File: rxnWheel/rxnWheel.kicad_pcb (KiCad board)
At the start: 2 copper layers, 1 part, among them IC1 TB9061AFNG,EL

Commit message: .
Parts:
- added D2: BZV55B12, Diode_SMD:D_MiniMELF, F.Cu at (208.8, 71.1)
- added D3: BZV55B12, Diode_SMD:D_MiniMELF, F.Cu at (200.3, 84.0)
- added D4: BZV55B12, Diode_SMD:D_MiniMELF, F.Cu at (247.5, 71.1)
- added D5: BZV55B12, Diode_SMD:D_MiniMELF, F.Cu at (239.0, 84.0)
- added D6: BZV55B12, Diode_SMD:D_MiniMELF, F.Cu at (228.1, 71.1)
- added D7: BZV55B12, Diode_SMD:D_MiniMELF, F.Cu at (219.7, 84.0)
- added Q1: IRF7458, Package_SO:SOIC-8_3.9x4.9mm_P1.27mm, F.Cu at (169.4, 72.7)
- added Q2: IRF7404, Package_SO:SOIC-8_3.9x4.9mm_P1.27mm, F.Cu at (201.4, 79.2)
- added Q3: Si4162DY, Package_SO:SOIC-8_3.9x4.9mm_P1.27mm, F.Cu at (201.4, 72.7)
- added Q4: IRF7404, Package_SO:SOIC-8_3.9x4.9mm_P1.27mm, F.Cu at (240.1, 79.2)
- added Q5: Si4162DY, Package_SO:SOIC-8_3.9x4.9mm_P1.27mm, F.Cu at (240.1, 72.7)
- added Q6: IRF7404, Package_SO:SOIC-8_3.9x4.9mm_P1.27mm, F.Cu at (220.7, 79.2)
- added Q7: Si4162DY, Package_SO:SOIC-8_3.9x4.9mm_P1.27mm, F.Cu at (220.7, 72.7)
- added R1: 100, Resistor_SMD:R_0805_2012Metric, F.Cu at (207.0, 91.3)
- added R10: 4K, Resistor_SMD:R_0805_2012Metric, F.Cu at (185.0, 73.9)
- added R11: 10K, Resistor_SMD:R_0805_2012Metric, F.Cu at (202.6, 94.3)
- added R12: 10K, Resistor_SMD:R_0805_2012Metric, F.Cu at (198.2, 91.3)
- added R13: 10K, Resistor_SMD:R_0805_2012Metric, F.Cu at (189.4, 71.0)
- added R14: 10K, Resistor_SMD:R_0805_2012Metric, F.Cu at (184.2, 71.0)
- added R15: 1K, Resistor_SMD:R_0805_2012Metric, F.Cu at (202.6, 97.2)
- added R16: 100, Resistor_SMD:R_0805_2012Metric, F.Cu at (202.6, 104.6)
- added R17: 100, Resistor_SMD:R_0805_2012Metric, F.Cu at (198.2, 107.6)
- added R18: 10K, Resistor_SMD:R_0805_2012Metric, F.Cu at (202.6, 107.6)
- added R19: 10K, Resistor_SMD:R_0805_2012Metric, F.Cu at (198.2, 104.6)
- added R2: 10K, Resistor_SMD:R_0805_2012Metric, F.Cu at (198.2, 94.3)
- added R20: 10K, Resistor_SMD:R_0805_2012Metric, F.Cu at (207.0, 104.6)
- added R21: 100, Resistor_SMD:R_0805_2012Metric, F.Cu at (221.1, 104.6)
- added R22: 100, Resistor_SMD:R_0805_2012Metric, F.Cu at (216.7, 107.6)
- added R23: 10K, Resistor_SMD:R_0805_2012Metric, F.Cu at (221.1, 107.6)
- added R24: 10K, Resistor_SMD:R_0805_2012Metric, F.Cu at (216.7, 104.6)
- added R25: 10K, Resistor_SMD:R_0805_2012Metric, F.Cu at (225.5, 104.6)
- added R26: 100, Resistor_SMD:R_0805_2012Metric, F.Cu at (223.9, 91.3)
- added R27: 100, Resistor_SMD:R_0805_2012Metric, F.Cu at (219.5, 94.3)
- added R28: 10K, Resistor_SMD:R_0805_2012Metric, F.Cu at (223.9, 94.3)
- added R29: 10K, Resistor_SMD:R_0805_2012Metric, F.Cu at (219.5, 91.3)
- added R3: 10K, Resistor_SMD:R_0805_2012Metric, F.Cu at (171.7, 77.4)
- added R30: 10K, Resistor_SMD:R_0805_2012Metric, F.Cu at (228.3, 91.3)
- added R4: 10K, Resistor_SMD:R_0805_2012Metric, F.Cu at (198.2, 97.2)
- added R5: 10K, Resistor_SMD:R_0805_2012Metric, F.Cu at (202.6, 91.3)
- added R6: 10K, Resistor_SMD:R_0805_2012Metric, F.Cu at (180.6, 77.4)
- added R7: 10K, Resistor_SMD:R_0805_2012Metric, F.Cu at (167.3, 77.4)
- added R8: 3m, Resistor_SMD:R_1206_3216Metric, F.Cu at (182.5, 97.0)
- added R9: 6K, Resistor_SMD:R_0805_2012Metric, F.Cu at (176.2, 77.4)
- added U1: ATmega328-P, Package_DIP:DIP-28_W7.62mm, F.Cu at (155.9, 71.6)
- added U2: MAX4373F, Package_SO:SO-8_3.9x4.9mm_P1.27mm, F.Cu at (177.8, 72.7)
- IC1: value TB9061AFNG,EL -> TB9061AFNG
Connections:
- net Net-(IC1-Pad23) renamed VReg
- net Net-(IC1-Pad4) renamed SHUTOFF
- IC1 pad 1: unconnected-(IC1-Pad1) -> Net-(IC1-Pad1)
- IC1 pad 10: unconnected-(IC1-Pad10) -> U_N
- IC1 pad 11: unconnected-(IC1-Pad11) -> V_N
- IC1 pad 12: unconnected-(IC1-Pad12) -> W_N
- IC1 pad 13: unconnected-(IC1-Pad13) -> U_P
- IC1 pad 14: unconnected-(IC1-Pad14) -> V_P
- IC1 pad 15: unconnected-(IC1-Pad15) -> W_P
- IC1 pad 17: unconnected-(IC1-Pad17) -> U_W
- IC1 pad 18: unconnected-(IC1-Pad18) -> V_W
- IC1 pad 19: unconnected-(IC1-Pad19) -> W_W
- IC1 pad 20: unconnected-(IC1-Pad20) -> WAVE_CMP
- IC1 pad 21: unconnected-(IC1-Pad21) -> Net-(IC1-Pad21)
- IC1 pad 22: unconnected-(IC1-Pad22) -> ASIG
- IC1 pad 5: Net-(IC1-Pad5) -> ASIG
- IC1 pad 6: Net-(IC1-Pad6) -> GND
- IC1 pad 7: unconnected-(IC1-Pad7) -> GND
- IC1 pad 8: unconnected-(IC1-Pad8) -> OUTFG

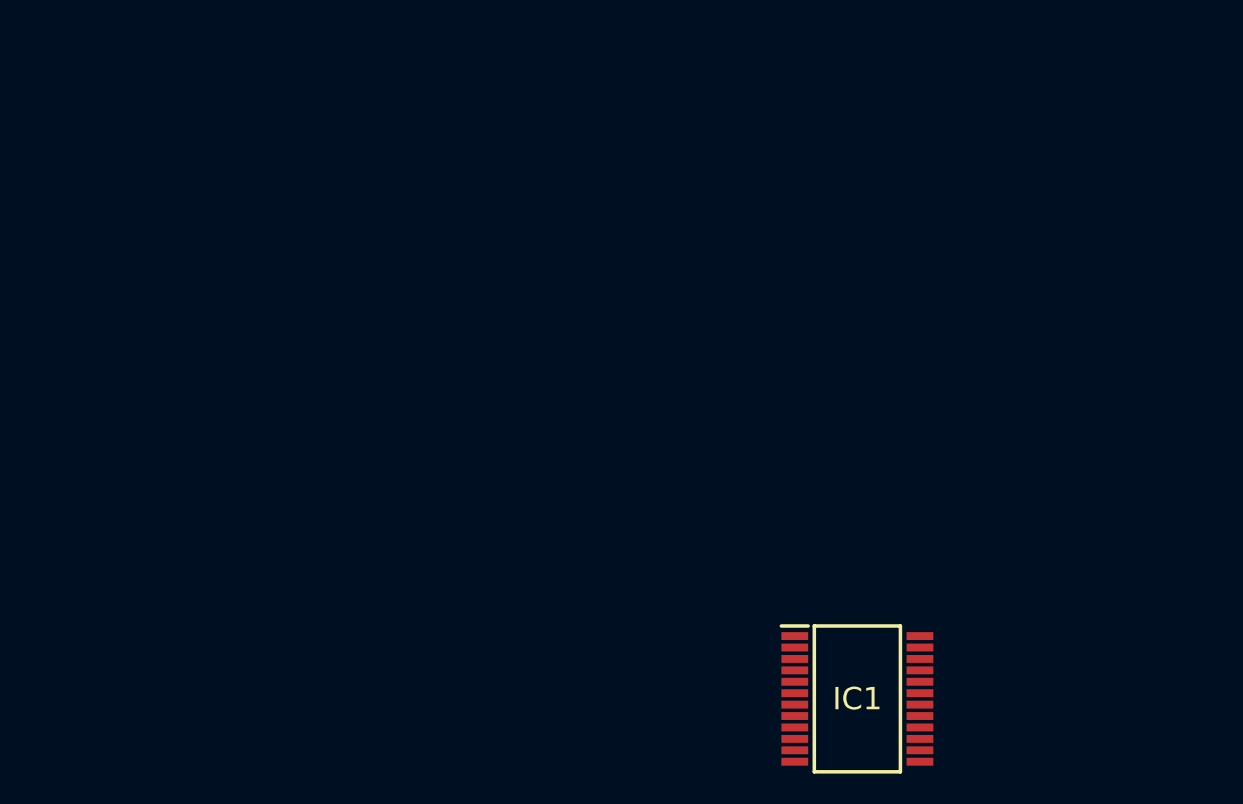
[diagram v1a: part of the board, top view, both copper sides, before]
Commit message: LED
led
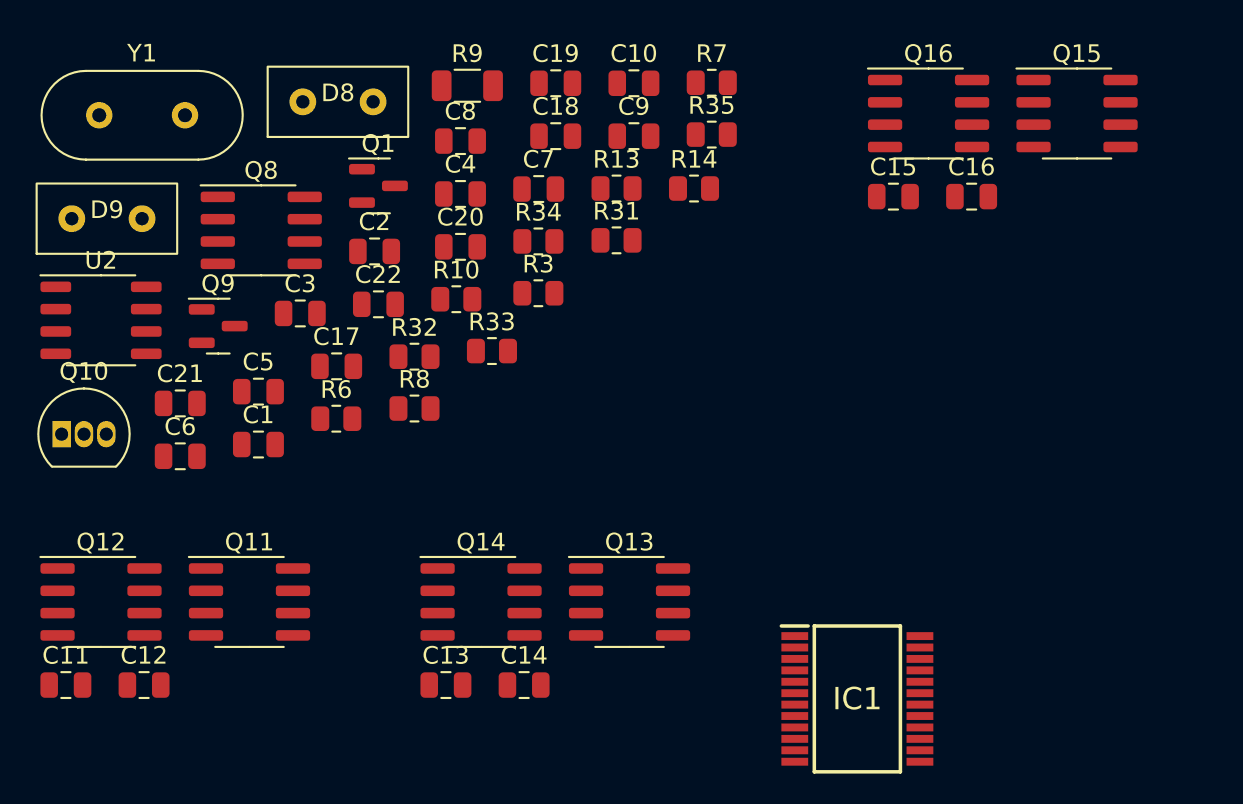
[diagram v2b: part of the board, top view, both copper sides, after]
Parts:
- added C1: 1uF, Capacitor_SMD:C_0805_2012Metric, F.Cu at (166.6, 43.9)
- added C10: 1uF, Capacitor_SMD:C_0805_2012Metric, F.Cu at (187.9, 23.4)
- added C11: 0.01uF, Capacitor_SMD:C_0805_2012Metric, F.Cu at (155.6, 57.6)
- added C12: 0.01uF, Capacitor_SMD:C_0805_2012Metric, F.Cu at (160.1, 57.6)
- added C13: 0.01uF, Capacitor_SMD:C_0805_2012Metric, F.Cu at (177.2, 57.6)
- added C14: 0.01uF, Capacitor_SMD:C_0805_2012Metric, F.Cu at (181.7, 57.6)
- added C15: 0.01uF, Capacitor_SMD:C_0805_2012Metric, F.Cu at (202.7, 29.8)
- added C16: 0.01uF, Capacitor_SMD:C_0805_2012Metric, F.Cu at (207.2, 29.8)
- added C17: 20pF, Capacitor_SMD:C_0805_2012Metric, F.Cu at (171.0, 39.5)
- added C18: 20pF, Capacitor_SMD:C_0805_2012Metric, F.Cu at (183.5, 26.4)
- added C19: 0.1uF, Capacitor_SMD:C_0805_2012Metric, F.Cu at (183.5, 23.4)
- added C2: 1nF, Capacitor_SMD:C_0805_2012Metric, F.Cu at (173.2, 33.0)
- added C20: 1uF, Capacitor_SMD:C_0805_2012Metric, F.Cu at (178.1, 32.7)
- added C21: 1uF, Capacitor_SMD:C_0805_2012Metric, F.Cu at (162.1, 41.6)
- added C22: 1uF, Capacitor_SMD:C_0805_2012Metric, F.Cu at (173.4, 36.0)
- added C3: 1uF, Capacitor_SMD:C_0805_2012Metric, F.Cu at (169.0, 36.5)
- added C4: 0.47 uF, Capacitor_SMD:C_0805_2012Metric, F.Cu at (178.1, 29.7)
- added C5: 0.1uF, Capacitor_SMD:C_0805_2012Metric, F.Cu at (166.6, 40.9)
- added C6: 0.01uF, Capacitor_SMD:C_0805_2012Metric, F.Cu at (162.1, 44.6)
- added C7: 0.1uF, Capacitor_SMD:C_0805_2012Metric, F.Cu at (182.5, 29.4)
- added C8: 1uF, Capacitor_SMD:C_0805_2012Metric, F.Cu at (178.1, 26.7)
- added C9: 1uF, Capacitor_SMD:C_0805_2012Metric, F.Cu at (187.9, 26.4)
- added D8: BPW20RF, TB9061AFNG:2x_jumper, F.Cu at (171.1, 24.4)
- added D9: LED, TB9061AFNG:2x_jumper, F.Cu at (157.9, 31.1)
- added Q1: 2N7002, Package_TO_SOT_SMD:SOT-23, F.Cu at (173.4, 29.2)
- added Q10: 2N3904, Package_TO_SOT_THT:TO-92_Inline, F.Cu at (155.4, 43.4)
- added Q11: Si4162DY, Package_SO:SOIC-8_3.9x4.9mm_P1.27mm, F.Cu at (166.1, 52.9)
- added Q12: IRF7404, Package_SO:SOIC-8_3.9x4.9mm_P1.27mm, F.Cu at (157.6, 52.9)
- added Q13: Si4162DY, Package_SO:SOIC-8_3.9x4.9mm_P1.27mm, F.Cu at (187.7, 52.9)
- added Q14: IRF7404, Package_SO:SOIC-8_3.9x4.9mm_P1.27mm, F.Cu at (179.2, 52.9)
- added Q15: Si4162DY, Package_SO:SOIC-8_3.9x4.9mm_P1.27mm, F.Cu at (213.2, 25.1)
- added Q16: IRF7404, Package_SO:SOIC-8_3.9x4.9mm_P1.27mm, F.Cu at (204.7, 25.1)
- added Q8: IRF7458, Package_SO:SOIC-8_3.9x4.9mm_P1.27mm, F.Cu at (166.7, 31.8)
- added Q9: 2N7002, Package_TO_SOT_SMD:SOT-23, F.Cu at (164.3, 37.2)
- added R10: 9.5K, Resistor_SMD:R_0805_2012Metric, F.Cu at (177.8, 35.7)
- added R13: 10K, Resistor_SMD:R_0805_2012Metric, F.Cu at (187.0, 29.4)
- added R14: 3K, Resistor_SMD:R_0805_2012Metric, F.Cu at (191.4, 29.4)
- added R3: 10K, Resistor_SMD:R_0805_2012Metric, F.Cu at (182.5, 35.3)
- added R31: 10K, Resistor_SMD:R_0805_2012Metric, F.Cu at (187.0, 32.3)
- added R32: 1K, Resistor_SMD:R_0805_2012Metric, F.Cu at (175.5, 38.9)
- added R33: 1K, Resistor_SMD:R_0805_2012Metric, F.Cu at (179.9, 38.6)
- added R34: 1K, Resistor_SMD:R_0805_2012Metric, F.Cu at (182.5, 32.4)
- added R35: 3m, Resistor_SMD:R_0805_2012Metric, F.Cu at (192.4, 26.3)
- added R6: 10K, Resistor_SMD:R_0805_2012Metric, F.Cu at (171.0, 42.5)
- added R7: 100, Resistor_SMD:R_0805_2012Metric, F.Cu at (192.4, 23.4)
- added R8: 10K, Resistor_SMD:R_0805_2012Metric, F.Cu at (175.5, 41.9)
- added R9: 3m, Resistor_SMD:R_1206_3216Metric, F.Cu at (178.5, 23.5)
- added U2: MAX4373F, Package_SO:SO-8_3.9x4.9mm_P1.27mm, F.Cu at (157.6, 36.9)
- added Y1: 16MHz, Crystal:Crystal_HC49-4H_Vertical, F.Cu at (157.5, 25.2)
- R11: value 10K -> 3K
- R12: value 10K -> 7K
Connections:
- net Net-(C1-Pad1) renamed +5V
- net U_MTR renamed Net-(Q11-Pad5)
- net V_MTR renamed Net-(Q15-Pad5)
- net W_MTR renamed Net-(Q13-Pad5)
- IC1 pad 22: ASIG -> VReg
- IC1 pad 5: ASIG -> SFCF
- R11 pad 2: ASIG -> SFCF
- R12 pad 1: ASIG -> SFCF
- U1 pad 1: unconnected-(U1-Pad1) -> RESET
- U1 pad 11: unconnected-(U1-Pad11) -> PWM_IN
- U1 pad 12: unconnected-(U1-Pad12) -> RSTMTRVOCP
- U1 pad 13: unconnected-(U1-Pad13) -> RSTMTRV
- U1 pad 14: unconnected-(U1-Pad14) -> SHUTOFF
- U1 pad 15: unconnected-(U1-Pad15) -> Net-(R7-Pad2)
- U1 pad 16: unconnected-(U1-Pad16) -> MTR_FRQ
- U1 pad 17: unconnected-(U1-Pad17) -> BTL1
- U1 pad 18: unconnected-(U1-Pad18) -> BTL2
- U1 pad 19: unconnected-(U1-Pad19) -> BTL3
- U1 pad 23: unconnected-(U1-Pad23) -> I_MOTOR_TELEM
- U1 pad 9: unconnected-(U1-Pad9) -> Net-(C17-Pad2)

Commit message: cleanup and corrections
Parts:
- added C2: 20pF, Capacitor_SMD:C_0805_2012Metric, F.Cu at (279.4, 71.1)
- added C3: 20pF, Capacitor_SMD:C_0805_2012Metric, F.Cu at (268.6, 101.6)
- added C4: 1uF, Capacitor_SMD:C_0805_2012Metric, F.Cu at (292.6, 64.5)
- added Q18: 2N3904, Package_TO_SOT_THT:TO-92_Inline, F.Cu at (312.4, 66.2)
- added Q20: 2N3904, Package_TO_SOT_THT:TO-92_Inline, F.Cu at (347.1, 66.2)
- added Q22: 2N3904, Package_TO_SOT_THT:TO-92_Inline, F.Cu at (329.8, 66.2)
- added R1: 100, Resistor_SMD:R_0805_2012Metric, F.Cu at (312.6, 70.2)
- added R11: 10K, Resistor_SMD:R_0805_2012Metric, F.Cu at (312.6, 73.2)
- added R12: 10K, Resistor_SMD:R_0805_2012Metric, F.Cu at (317.1, 70.2)
- added R15: 100, Resistor_SMD:R_0805_2012Metric, F.Cu at (347.3, 70.2)
- added R16: 100, Resistor_SMD:R_0805_2012Metric, F.Cu at (347.3, 76.1)
- added R17: 10K, Resistor_SMD:R_0805_2012Metric, F.Cu at (353.8, 64.4)
- added R2: 100, Resistor_SMD:R_0805_2012Metric, F.Cu at (312.6, 76.1)
- added R21: 10K, Resistor_SMD:R_0805_2012Metric, F.Cu at (351.7, 73.2)
- added R22: 10K, Resistor_SMD:R_0805_2012Metric, F.Cu at (347.3, 73.2)
- added R26: 10K, Resistor_SMD:R_0805_2012Metric, F.Cu at (351.7, 70.2)
- added R27: 100, Resistor_SMD:R_0805_2012Metric, F.Cu at (330.0, 70.2)
- added R35: 100, Resistor_SMD:R_0805_2012Metric, F.Cu at (330.0, 76.1)
- added R36: 10K, Resistor_SMD:R_0805_2012Metric, F.Cu at (336.5, 64.4)
- added R37: 10K, Resistor_SMD:R_0805_2012Metric, F.Cu at (334.4, 73.2)
- added R38: 10K, Resistor_SMD:R_0805_2012Metric, F.Cu at (330.0, 73.2)
- added R39: 10K, Resistor_SMD:R_0805_2012Metric, F.Cu at (334.4, 70.2)
- added R4: 10K, Resistor_SMD:R_0805_2012Metric, F.Cu at (319.2, 64.4)
- added R40: 10K, Resistor_SMD:R_0805_2012Metric, F.Cu at (279.4, 74.1)
- added R41: 33K, Resistor_SMD:R_0805_2012Metric, F.Cu at (292.5, 67.5)
- added R42: 33K, Resistor_SMD:R_0805_2012Metric, F.Cu at (288.2, 71.1)
- added R43: 33K, Resistor_SMD:R_0805_2012Metric, F.Cu at (283.8, 71.1)
- added R44: 10K, Resistor_SMD:R_0805_2012Metric, F.Cu at (297.0, 64.4)
- added R45: 10K, Resistor_SMD:R_0805_2012Metric, F.Cu at (279.4, 77.0)
- added R46: 10K, Resistor_SMD:R_0805_2012Metric, F.Cu at (273.0, 101.6)
- added R47: 33K, Resistor_SMD:R_0805_2012Metric, F.Cu at (283.8, 74.1)
- added R48: 33K, Resistor_SMD:R_0805_2012Metric, F.Cu at (268.5, 104.6)
- added R49: 33K, Resistor_SMD:R_0805_2012Metric, F.Cu at (279.4, 80.0)
- added R5: 10K, Resistor_SMD:R_0805_2012Metric, F.Cu at (317.1, 73.2)
- added U3: Pad, TB9061AFNG:Pad, F.Cu at (256.5, 48.3)
- added U4: Pad, TB9061AFNG:Pad, F.Cu at (266.8, 48.3)
- added U5: Pad, TB9061AFNG:Pad, F.Cu at (261.7, 48.3)
- added U6: ATmega328-P, Package_DIP:DIP-28_W7.62mm, F.Cu at (267.9, 65.0)
- added Y2: 16MHz, Crystal:Crystal_HC49-4H_Vertical, F.Cu at (281.3, 66.3)
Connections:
- C11 pad 2: I_SENSE -> GND
- C13 pad 2: I_SENSE -> GND
- C15 pad 2: I_SENSE -> GND
- D2 pad 2: I_SENSE -> GND
- D4 pad 2: I_SENSE -> GND
- D6 pad 2: I_SENSE -> GND
- Q3 pad 1: I_SENSE -> GND
- Q3 pad 2: I_SENSE -> GND
- Q3 pad 3: I_SENSE -> GND
- Q5 pad 1: I_SENSE -> GND
- Q5 pad 2: I_SENSE -> GND
- Q5 pad 3: I_SENSE -> GND
- Q7 pad 1: I_SENSE -> GND
- Q7 pad 2: I_SENSE -> GND
- Q7 pad 3: I_SENSE -> GND
- R18 pad 2: I_SENSE -> GND
- R23 pad 2: I_SENSE -> GND
- R28 pad 2: I_SENSE -> GND
